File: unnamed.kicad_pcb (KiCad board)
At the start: 2 copper layers, 140 x 95 mm, 29 parts, among them J1 C128990, J2 C128990, SW1 KeySwitch, SW10 KeySwitch, SW11 KeySwitch, SW12 KeySwitch, SW13 KeySwitch, SW14 KeySwitch, SW15 KeySwitch, SW16 KeySwitch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

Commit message: update pcb and project, new 3d file for cases.
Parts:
- moved J1 0.19 mm to (218.4, 116.5)
- moved J2 0.19 mm to (218.4, 116.5)
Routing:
- net /U0RX: track 26.0 -> 23.3 mm
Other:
- board text added: "case cut place for TRRS connector"
- board text added: "case cut place for USB connector"
- board text added: "origin of gerber"

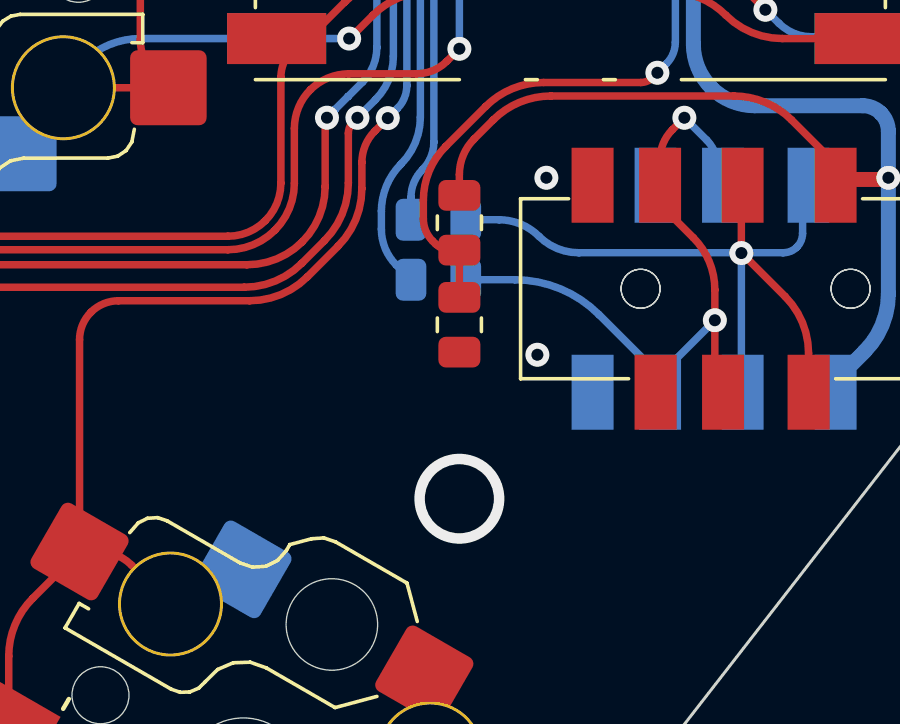
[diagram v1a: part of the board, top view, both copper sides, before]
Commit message: add parameter info in pcb in user layer modify case model with parameters add Edge_Cuts dxf file add case.stl
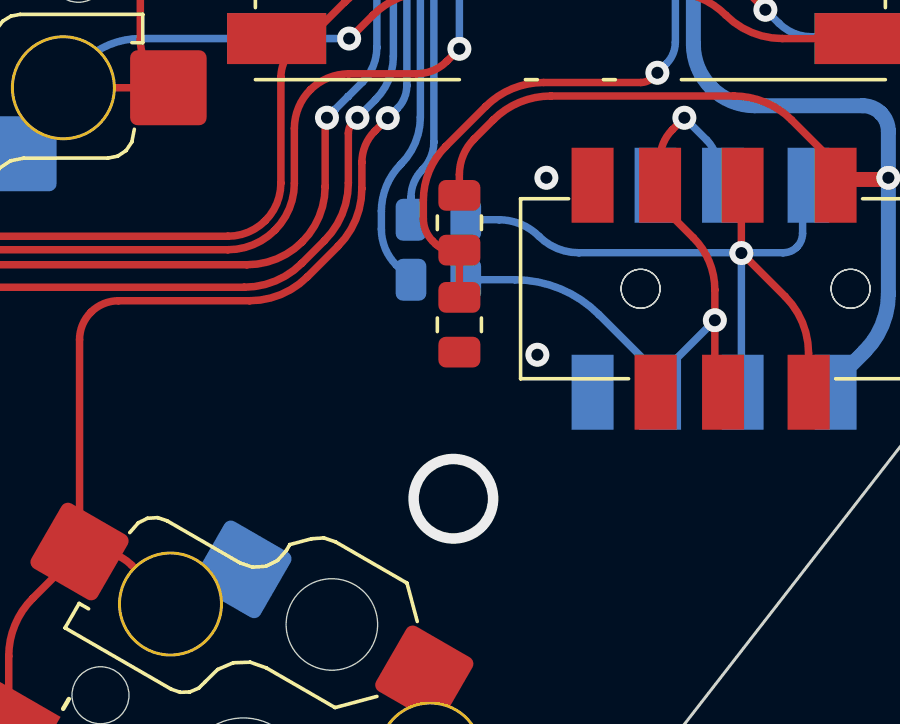
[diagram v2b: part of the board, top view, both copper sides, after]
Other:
- board text added: "-trrs_cut_y"
- board text added: "board_height"
- board text added: "board_width"
- board text added: "trrs_cut_height"
- board text added: "trrs_cut_width"
- board text added: "trrs_cut_x"
- board text added: "type_c_cut_height"
- board text added: "type_c_cut_width"
- board text added: "type_c_cut_x"
